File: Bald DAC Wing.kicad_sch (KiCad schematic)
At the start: 42 parts, among them J1 Power_In, J2 DAC_A_Out, J3 DAC_B_Out, U1 AD5447, U2 AD8065ARTZ, U3 AD8065ARTZ, U4 74LVC574APWR, U5 74LVC574APWR, U6 74LVC14, U7 REF3425

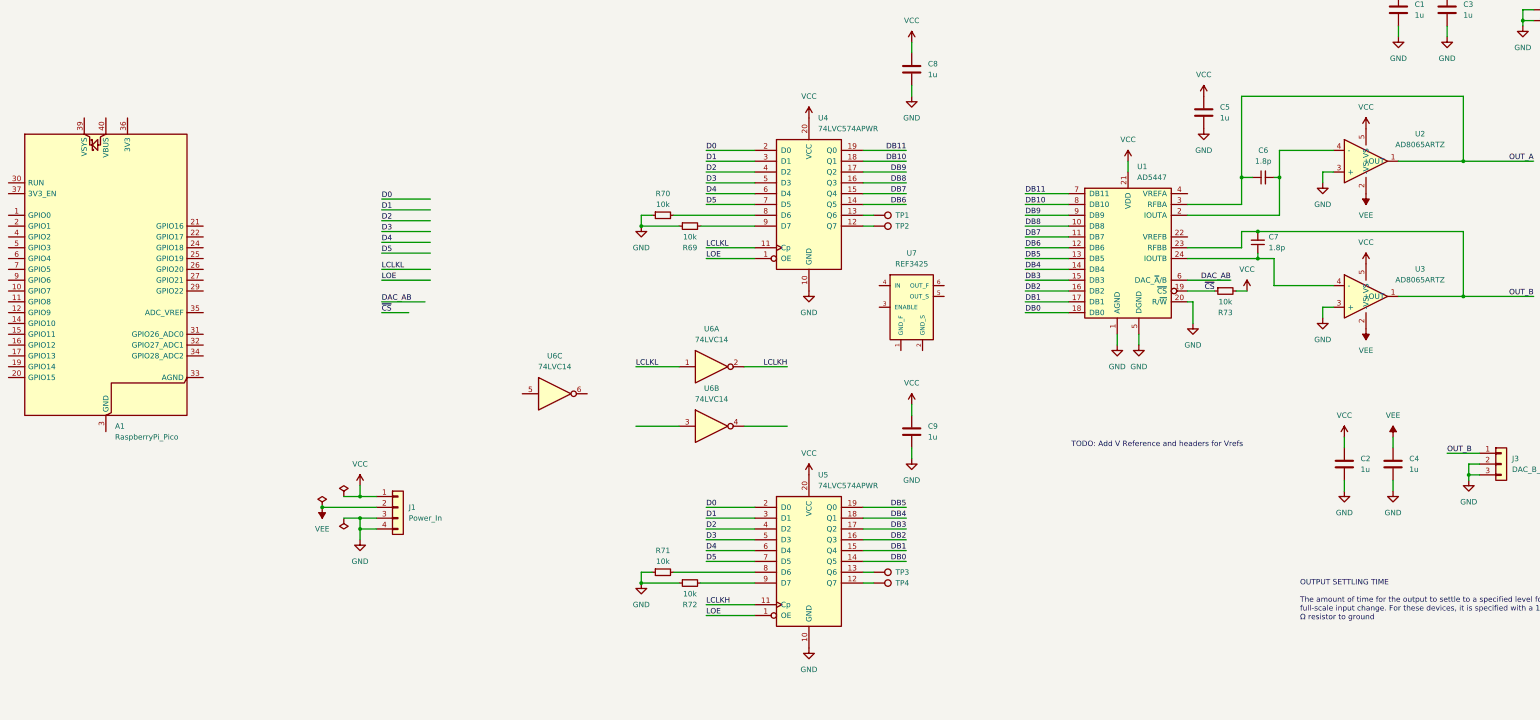
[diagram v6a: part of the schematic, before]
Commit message: added a reference circuit. still need to change the cap values
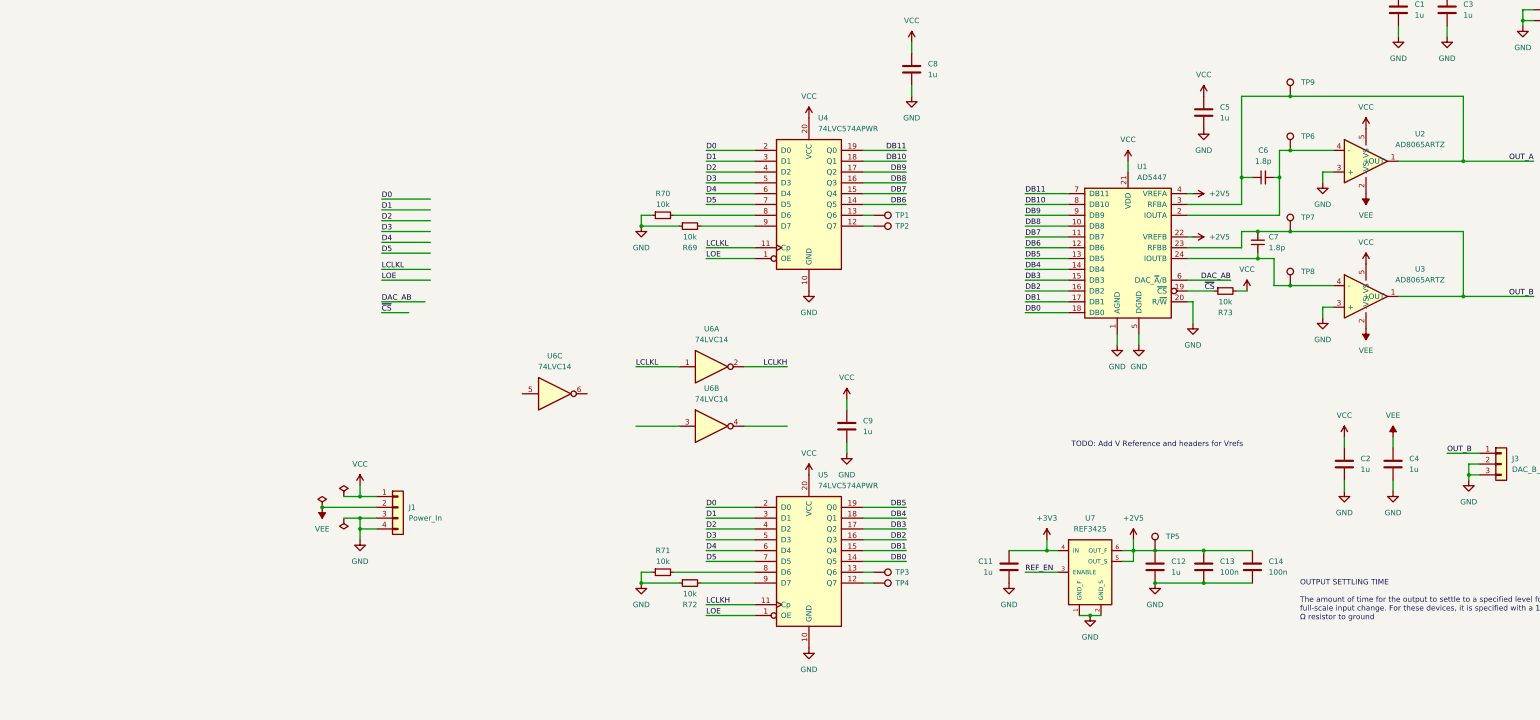
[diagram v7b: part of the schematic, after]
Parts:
- removed A1: RaspberryPi_Pico, Module:RaspberryPi_Pico_Common_Unspecified, symbol MCU_Module:RaspberryPi_Pico
- added C11, C12: 1u, Capacitor_SMD:C_0805_2012Metric_Pad1.18x1.45mm_HandSolder, symbol Device:C
- added C13, C14: 100n, Capacitor_SMD:C_0805_2012Metric_Pad1.18x1.45mm_HandSolder, symbol Device:C
- added TP5, TP6, TP7, TP8, TP9: TestPoint_Harwin, My Libraries:Harwin-S1751-46-Test-Point, symbol My Library:TestPoint_Harwin
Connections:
- net GND: now also U7.1 (GND_F), U7.2 (GND_S), C11.2, C12.2, C13.2, C14.2
- net OUT_A: now also TP9.1
- net OUT_B: now also TP7.1
- net at C6.2, U1.2 (IOUTA), U2.4 (-): now also TP6.1
- net +2V5: now reaches U1.22 (VREFB)
- net +2V5: now also U1.4 (VREFA), U7.5 (OUT_S), U7.6 (OUT_F), C12.1, C13.1, C14.1, TP5.1
- net at C7.1, U1.24 (IOUTB), U3.4 (-): now also TP8.1
- net REF_EN: now reaches U7.3 (ENABLE)
- net +3V3: now reaches U7.4 (IN)
- net +3V3: now also C11.1
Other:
- moved on the sheet: C9, U7

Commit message: clanker is finaly working
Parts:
- U7: LCSC [C187836](https://www.lcsc.com/product-detail/C187836.html?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 -> C187836
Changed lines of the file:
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@@
 			)
 		)
-		(property "LCSC" "[C187836](https://www.lcsc.com/product-detail/C187836.html?s_z=n_q_REF3425&spm=wm.fly.bg.0.cbh&lcsc_vid=Q1AIUQJRT1INXgYEFVQKUgEDQAUMX1xSElRZVFxRFFMxVlNeT1VeV1ZfT1RbVTsOAxUeFF5JWBYZEEoKFBINSQcJGk4%3D \"C187836\")"
+		(property "LCSC" "C187836"
 			(at 284.48 171.45 0)
 			(hide yes)
